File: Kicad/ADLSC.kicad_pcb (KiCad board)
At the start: 2 copper layers, 137.2 x 61 mm, 62 parts, among them J1 Weidmueller 1824810000 or 176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, J2 Weidmueller 1824810000 or 176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, J3 Weidmueller 1824810000 or 176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, J4 Weidmueller 1824810000 or 176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, J5 Pmod host I2C, J6 Pmod host SPI, Q1 AOD442, Q2 MMBT2222, Q3 TSM160P02CS, Q4 TSM160P02CS, U1 74AHCT125D, U3 MAX809M

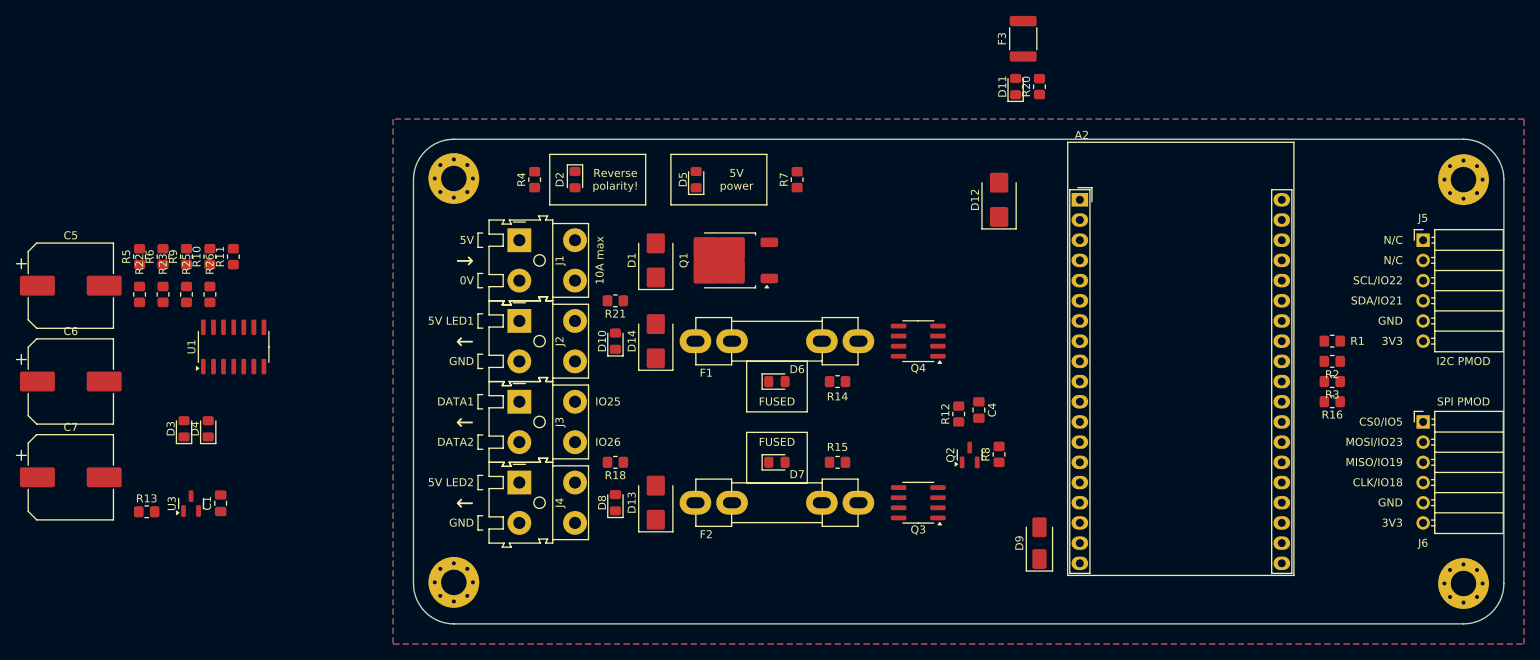
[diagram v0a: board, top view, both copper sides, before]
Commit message: Route PCB.
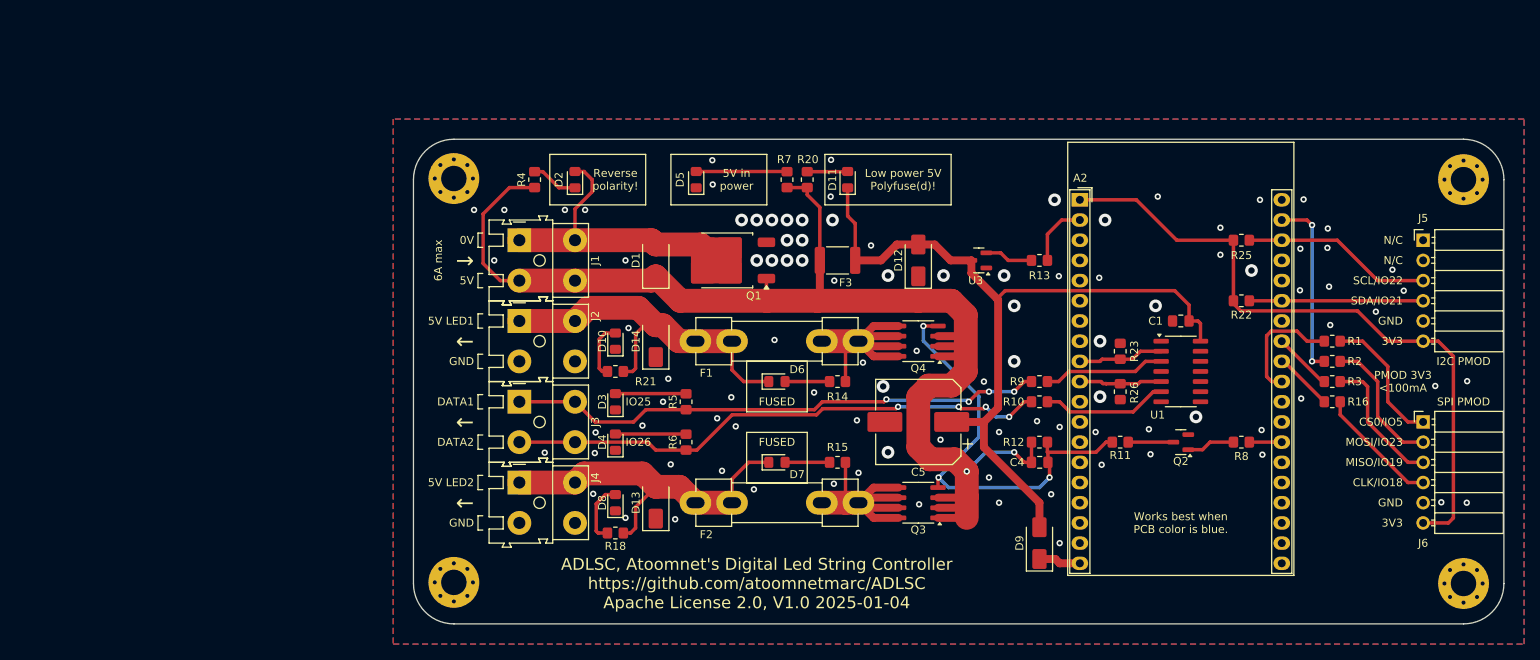
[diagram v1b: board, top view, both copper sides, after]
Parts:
- removed C6, C7: 16V 470uF, Capacitor_SMD:CP_Elec_10x10.5
- added REF**: WEEE-Logo_21x30mm_SilkScreen, Symbol:WEEE-Logo_21x30mm_SilkScreen, B.Cu at (96.5, 33.6)
- D1, D12, D13, D14: footprint Diode_SMD:D_SMB -> Diode_SMD:D_SMA
- moved R22 138.6 mm to (104.1, 20.3), turned to 180 degrees
- moved R25 132.9 mm to (104.1, 12.7), turned to 180 degrees
- moved C1 122.9 mm to (96.5, 22.9), turned to 180 degrees
- moved R23 120.6 mm to (88.9, 26.7)
- moved U1 119.2 mm to (96.5, 29.2), turned to 0 degrees
- moved R13 116.7 mm to (78.7, 15.2)
- moved R26 115.2 mm to (88.9, 31.8), turned to -90 degrees
- moved R11 114.0 mm to (88.9, 38.1), turned to 180 degrees
- moved R9 108.4 mm to (78.7, 30.5), turned to 180 degrees
- moved C5 108.0 mm to (63.5, 35.6), turned to 180 degrees
- moved R10 105.9 mm to (78.7, 33.0), turned to 180 degrees
- moved U3 103.7 mm to (71.1, 15.2), turned to 180 degrees
- moved R5 71.1 mm to (34.3, 33.0)
- moved R6 69.8 mm to (34.3, 38.1)
- moved D3 54.4 mm to (25.4, 33.0)
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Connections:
- D1 pad 1: /0V_IN -> +5V_IN
- D1 pad 2: +5V_IN -> /0V_IN
- J1 pad 1: +5V_IN -> /0V_IN
- J1 pad 2: /0V_IN -> +5V_IN
- R5 pad 1: Net-(R5-Pad1) -> DATA1
- R6 pad 1: Net-(R10-Pad1) -> DATA2
- R9 pad 1: Net-(R5-Pad1) -> Net-(R9-Pad1)
- U1 pad 3: Net-(R5-Pad1) -> Net-(R9-Pad1)
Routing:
- net +5V_IN: track 0.00 -> 162.9 mm, vias 0 -> 2
- net +5V: track 0.00 -> 99.6 mm
- net +3.3V: track 0.00 -> 84.2 mm
- net DATA2: track 0.00 -> 68.6 mm, vias 0 -> 4
- net DATA1: track 0.00 -> 67.8 mm, vias 0 -> 4
- net Net-(Q3-G): track 0.00 -> 55.4 mm, vias 0 -> 3
- net +5V_LED1: track 0.00 -> 47.0 mm
- net +5V_LED2: track 0.00 -> 45.3 mm
- net /0V_IN: track 0.00 -> 37.0 mm
- net Net-(F1-Pad1): track 0.00 -> 32.0 mm
- net Net-(F2-Pad1): track 0.00 -> 32.0 mm
- net SCL: track 0.00 -> 24.0 mm
- net MOSI: track 0.00 -> 22.8 mm, vias 0 -> 2
- net SDA: track 0.00 -> 21.9 mm
- net Net-(J6-~{CS}): track 0.00 -> 17.2 mm
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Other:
- board text added: "${TITLE} ${COMPANY} ${COMMENT1}, ${REVISION} ${ISSUE_DATE}"
- board text added: "5V in power"
- board text added: "6A max"
- board text added: "Low power 5V Polyfuse(d)!"
- board text added: "PMOD 3V3 <100mA"
- board text added: "Works best when PCB color is blue."
- board text removed: "10A max"
- board text removed: "5V power"

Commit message: Finalize pcb. Add gerbers. Add more readme.
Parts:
- removed REF**: WEEE-Logo_21x30mm_SilkScreen, Symbol:WEEE-Logo_21x30mm_SilkScreen
- F2: renamed from F1; value 5x20mm 3A slow blow -> 2x fuseholder PCB clip with T3AL250V 5x20mm 3A slow blow fuse
- F3: renamed from F2; value 5x20mm 3A slow blow -> 2x fuseholder PCB clip with T3AL250V 5x20mm 3A slow blow fuse
- renumbered A2 to A1, C5 to C2, C4 to C3, D2 to D1, D4 to D10, D7 to D11, D8 to D12, D9 to D14, D5 to D2, D11 to D3, D1 to D4, D12 to D5, D10 to D6, D14 to D7, D6 to D8, D3 to D9, F3 to F1, J5 to J2, J2 to J3, J3 to J4, J6 to J5, J4 to J6, Q4 to Q2, Q2 to Q3, Q3 to Q4, R4 to R1, R21 to R10, R14 to R11, R9 to R12, R3 to R13, R26 to R14, R5 to R15, R10 to R16, R16 to R17, R6 to R18, R12 to R19, R7 to R2, R11 to R20, R8 to R21, R15 to R22, R18 to R23, R20 to R3, R25 to R4, R13 to R5, R22 to R6, R1 to R7, R23 to R8, R2 to R9, U3 to U1, U1 to U2
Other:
- board text added: "ESP32-DevKitC + ESP32-WROVER-E"
- board text added: "Relay: IO4 active high"
